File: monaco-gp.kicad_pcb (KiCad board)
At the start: 2 copper layers, 124.8 x 102.7 mm, 4 parts

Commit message: routing
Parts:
- moved F1 70.9 mm to (52.7, 187.9)
- moved E1 51.2 mm to (52.8, 99.9)
- moved C1 22.2 mm to (52.9, 115.1)
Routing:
- net /Y1: track 36.2 -> 191.8 mm, vias 0 -> 1
- net /Y29: track 36.2 -> 191.1 mm, vias 0 -> 1
- net /Y2: track 36.2 -> 189.6 mm, vias 0 -> 1
- net /Y3: track 36.2 -> 187.2 mm, vias 0 -> 1
- net /Y4: track 36.2 -> 185.5 mm, vias 0 -> 1
- net /Y5: track 36.2 -> 183.6 mm, vias 0 -> 1
- net /Y30: track 36.2 -> 182.0 mm, vias 0 -> 1
- net /Y6: track 36.2 -> 181.1 mm, vias 0 -> 1
- net /Y7: track 36.2 -> 178.6 mm, vias 0 -> 1
- net /X23: track 36.0 -> 177.1 mm, vias 0 -> 3
- net /Y8: track 36.2 -> 175.4 mm, vias 0 -> 1
- net /Y31: track 36.2 -> 173.0 mm, vias 0 -> 1
- net /Y32: track 36.2 -> 170.2 mm, vias 0 -> 1
- net /X24: track 37.8 -> 171.4 mm, vias 0 -> 3
- net /Y9: track 36.2 -> 168.9 mm, vias 0 -> 1
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- added copper zone on B.Cu, net /L2
- added copper zone on F.Cu, net /L2
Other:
- board size 124.8 x 102.7 mm -> 124.9 x 173.6 mm
- board text added: "B1"
- board text added: "B22"
- board text added: "EA"
- board text added: "EZ"
- board text added: "あ"

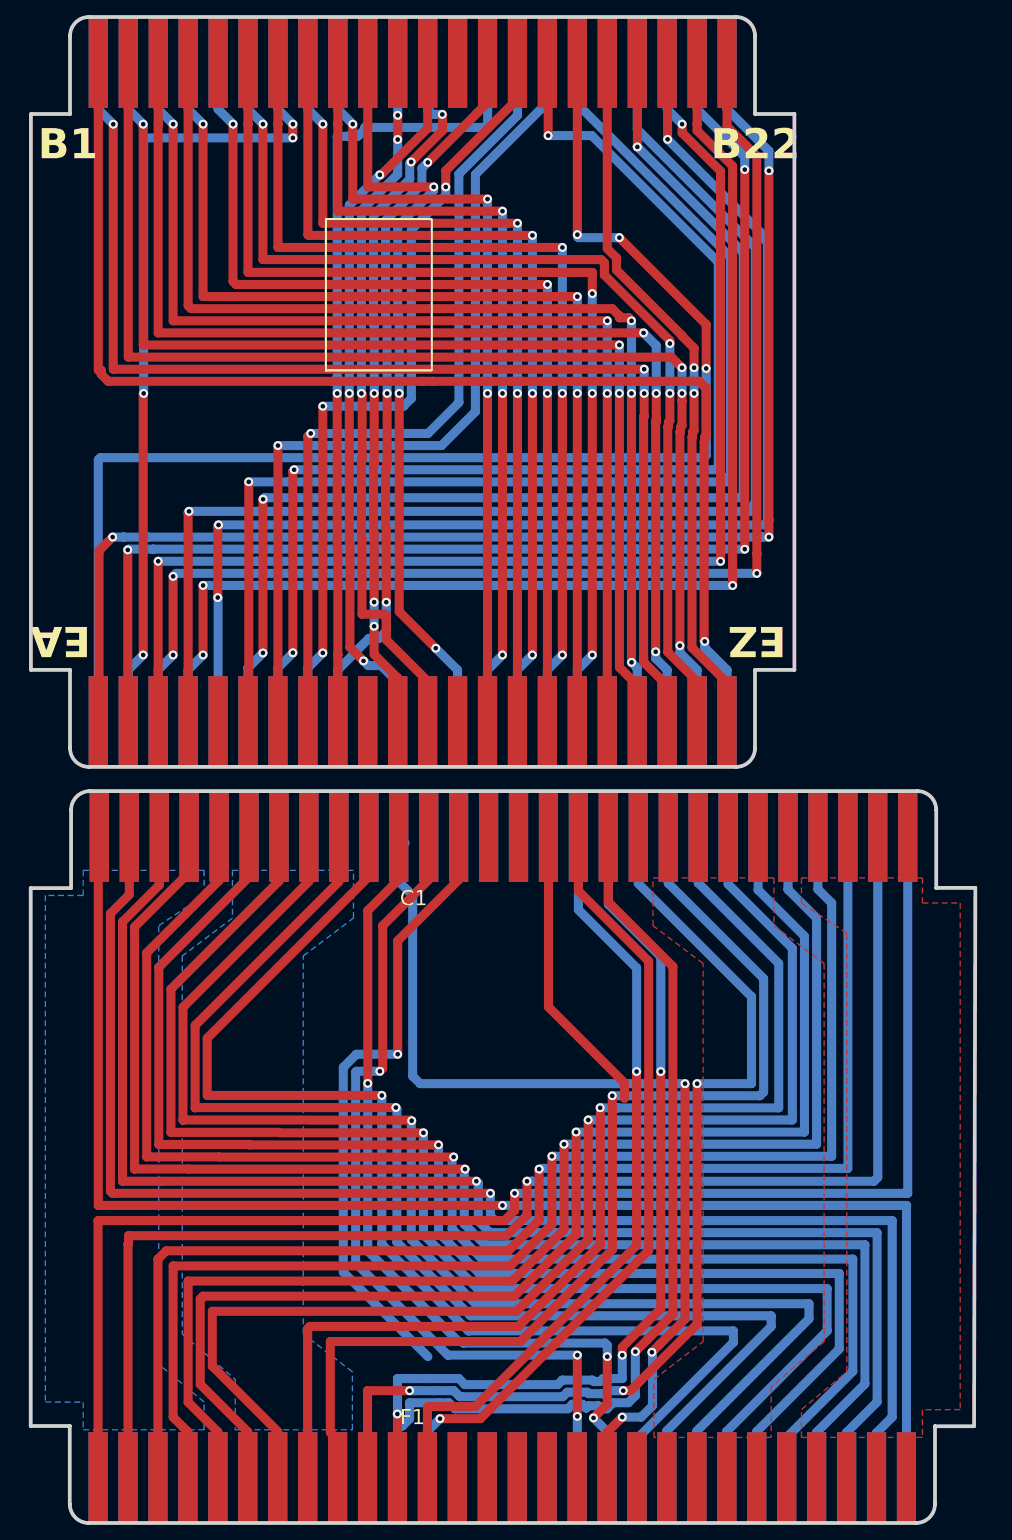
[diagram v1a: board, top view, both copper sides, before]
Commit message: fixed footprints again. 22-pin board should be okay now :)
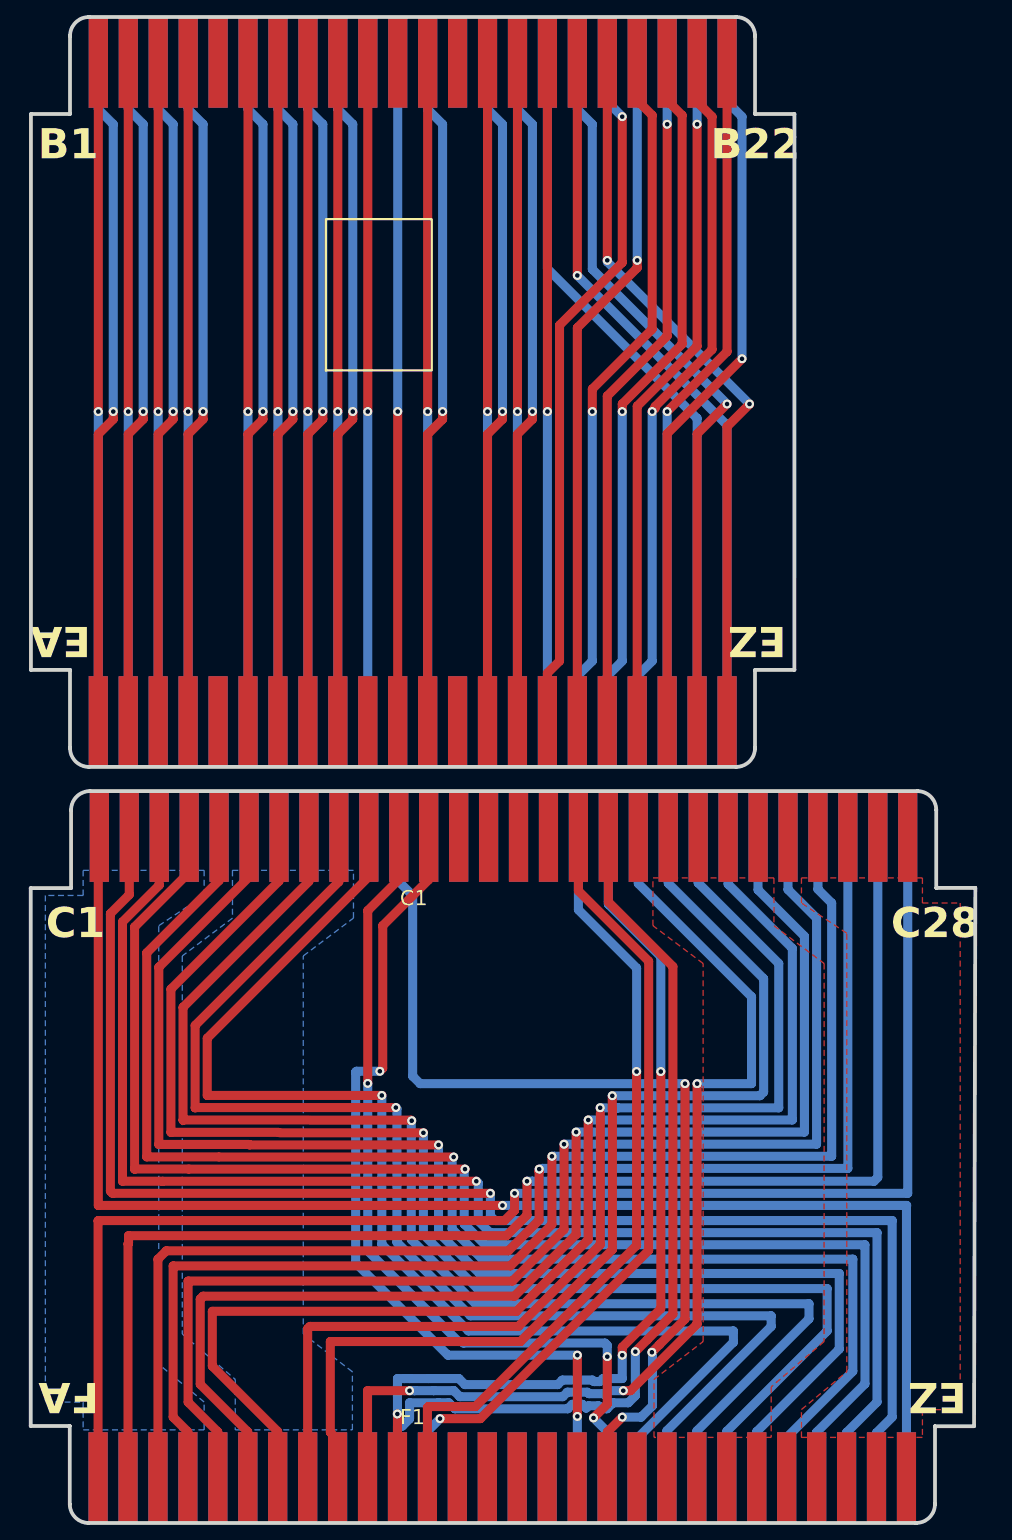
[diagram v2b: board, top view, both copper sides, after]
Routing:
- net /X23: track 177.1 -> 88.8 mm, vias 3 -> 1
- net /Y13: track 83.0 -> 0.00 mm, vias 1 -> 0
- net /X24: track 171.4 -> 88.8 mm, vias 3 -> 1
- net /X22: track 177.5 -> 95.4 mm, vias 3 -> 1
- net /X1: track 167.3 -> 87.2 mm
- net /X26: track 168.5 -> 88.8 mm
- net /X25: track 164.5 -> 88.8 mm, vias 3 -> 1
- net /X20: track 166.0 -> 90.5 mm, vias 3 -> 1
- net /X18: track 165.3 -> 92.1 mm, vias 3 -> 1
- net /X2: track 160.0 -> 87.2 mm, vias 3 -> 1
- net /X28: track 159.1 -> 88.8 mm
- net /X16: track 156.9 -> 87.2 mm, vias 3 -> 1
- net /X19: track 159.4 -> 92.1 mm, vias 3 -> 1
- net /X42: track 158.9 -> 92.1 mm, vias 3 -> 1
- net /X3: track 152.1 -> 87.2 mm, vias 3 -> 1
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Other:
- board text added: "BA"
- board text added: "BZ"
- board text added: "C1"
- board text added: "C28"
- board text added: "CA"
- board text added: "CZ"
- board text added: "E1"
- board text added: "E22"
- board text added: "F1"
- board text added: "F28"
- board text added: "FA"
